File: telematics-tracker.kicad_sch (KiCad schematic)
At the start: 0 parts

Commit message: M2: mcu ERC-clean
mcu.kicad_sch: AT32F403ACGT7 with all 48 pins wired per handoff section 5,
verified 48/48 against the exported netlist by tools/checkpins.py.

Contents: 8 MHz HSE (Crystal_GND24 + 2x18pF), 32.768 kHz LSE (+2x6.8pF),
NRST 100nF, BOOT0 10k + solder-jumper to 3V3, BOOT1/PB2 10k pulldown,
VBAT via 0R from 3V3 + 100nF, VDDA ferrite + 1uF/100nF, 100nF per VDD pin
+ 4.7uF bulk, PC13 heartbeat LED, PB11 network LED via MMBT3904, U3
QMI8658B IMU on I2C1 with 2.2k pull-ups, and test points on SWD, both
debug UART lines, reset and the rails.

ERC: 0 errors. 51 warnings, all isolated_pin_label on root sheet pins that
only this sheet exposes so far; they resolve as storage/io/modem_rf land.

Generator fixes needed to get here (all now guarded in schgen.py):
  - power symbols must be in_bom/on_board yes, else their pins read as
    unconnected
  - power-symbol references must be unique project-wide, not per sheet
  - (property private ...) is valid in a schematic; stripping it caused a
    spurious lib_symbol_mismatch
  - added a net-collision detector: it caught R3 and FB1 stubs both landing
    on (88.9, 88.9), which had silently merged VBAT_MCU into 3V3 and shorted
    MCU pin 1 to pin 48

Co-Authored-By: Claude Fable 5 <noreply@anthropic.com>
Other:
- added sheet mcu (mcu.kicad_sch)
- note added: "Remove them when the power sheet is added."
- note added: "TEMPORARY: the PWR_FLAG symbols below mark rails that will be driven by"
- note added: "power.kicad_sch (not yet drawn - pending the buck selection decision)."

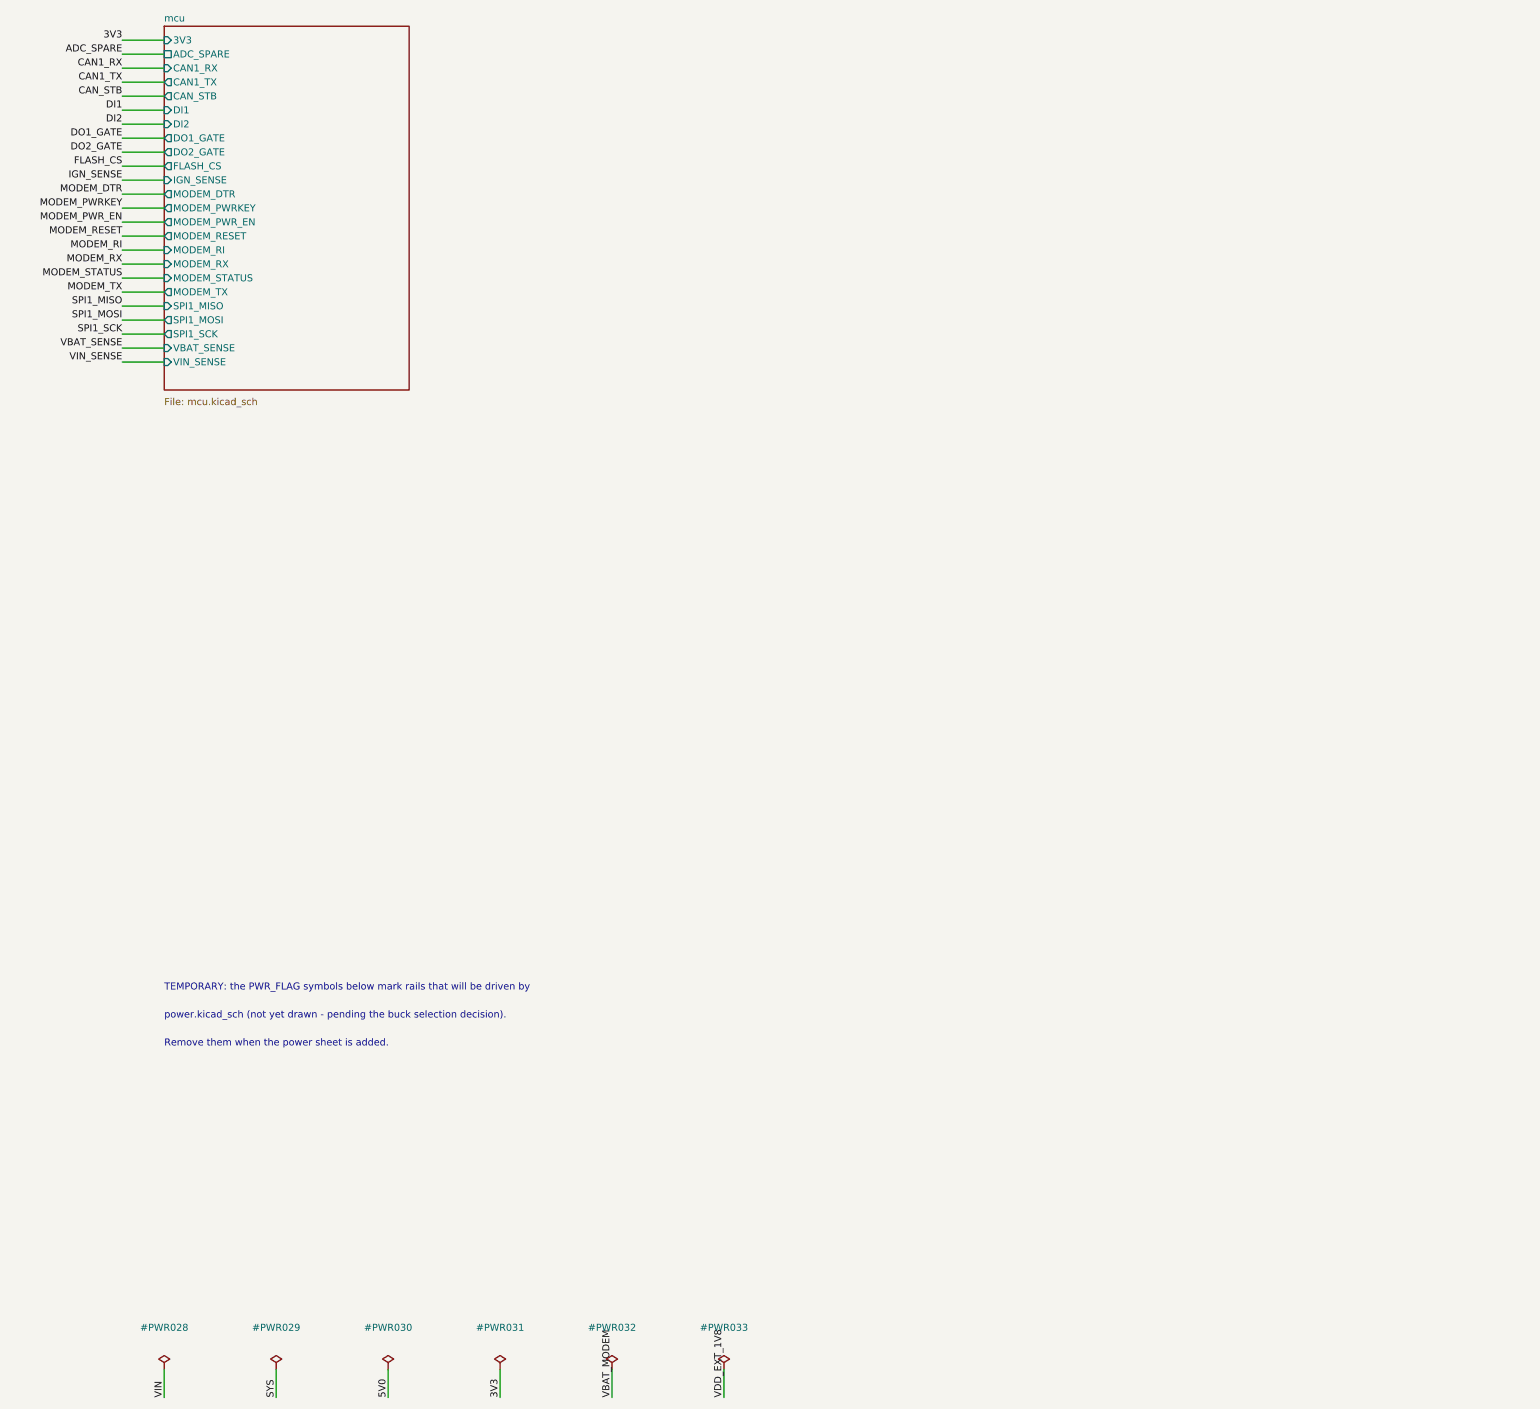
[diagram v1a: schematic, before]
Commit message: M2: storage ERC-clean
U7 GD25Q64ESIGR (C2831359, tape and reel per F-3) on SPI1: CS=PA4 via
FLASH_CS, SCK/MOSI/MISO to SPI1_*, WP# and HOLD# tied 3V3, 100nF + 1uF.
W25Q64JVSSIQ alternate recorded in the symbol's Alternate field.

Root inter-sheet plumbing switched from plain labels to global labels:
two same-named plain labels attached to sheet pins on different sheets are
reported dangling rather than merging. ERC 0 errors.

Co-Authored-By: Claude Fable 5 <noreply@anthropic.com>
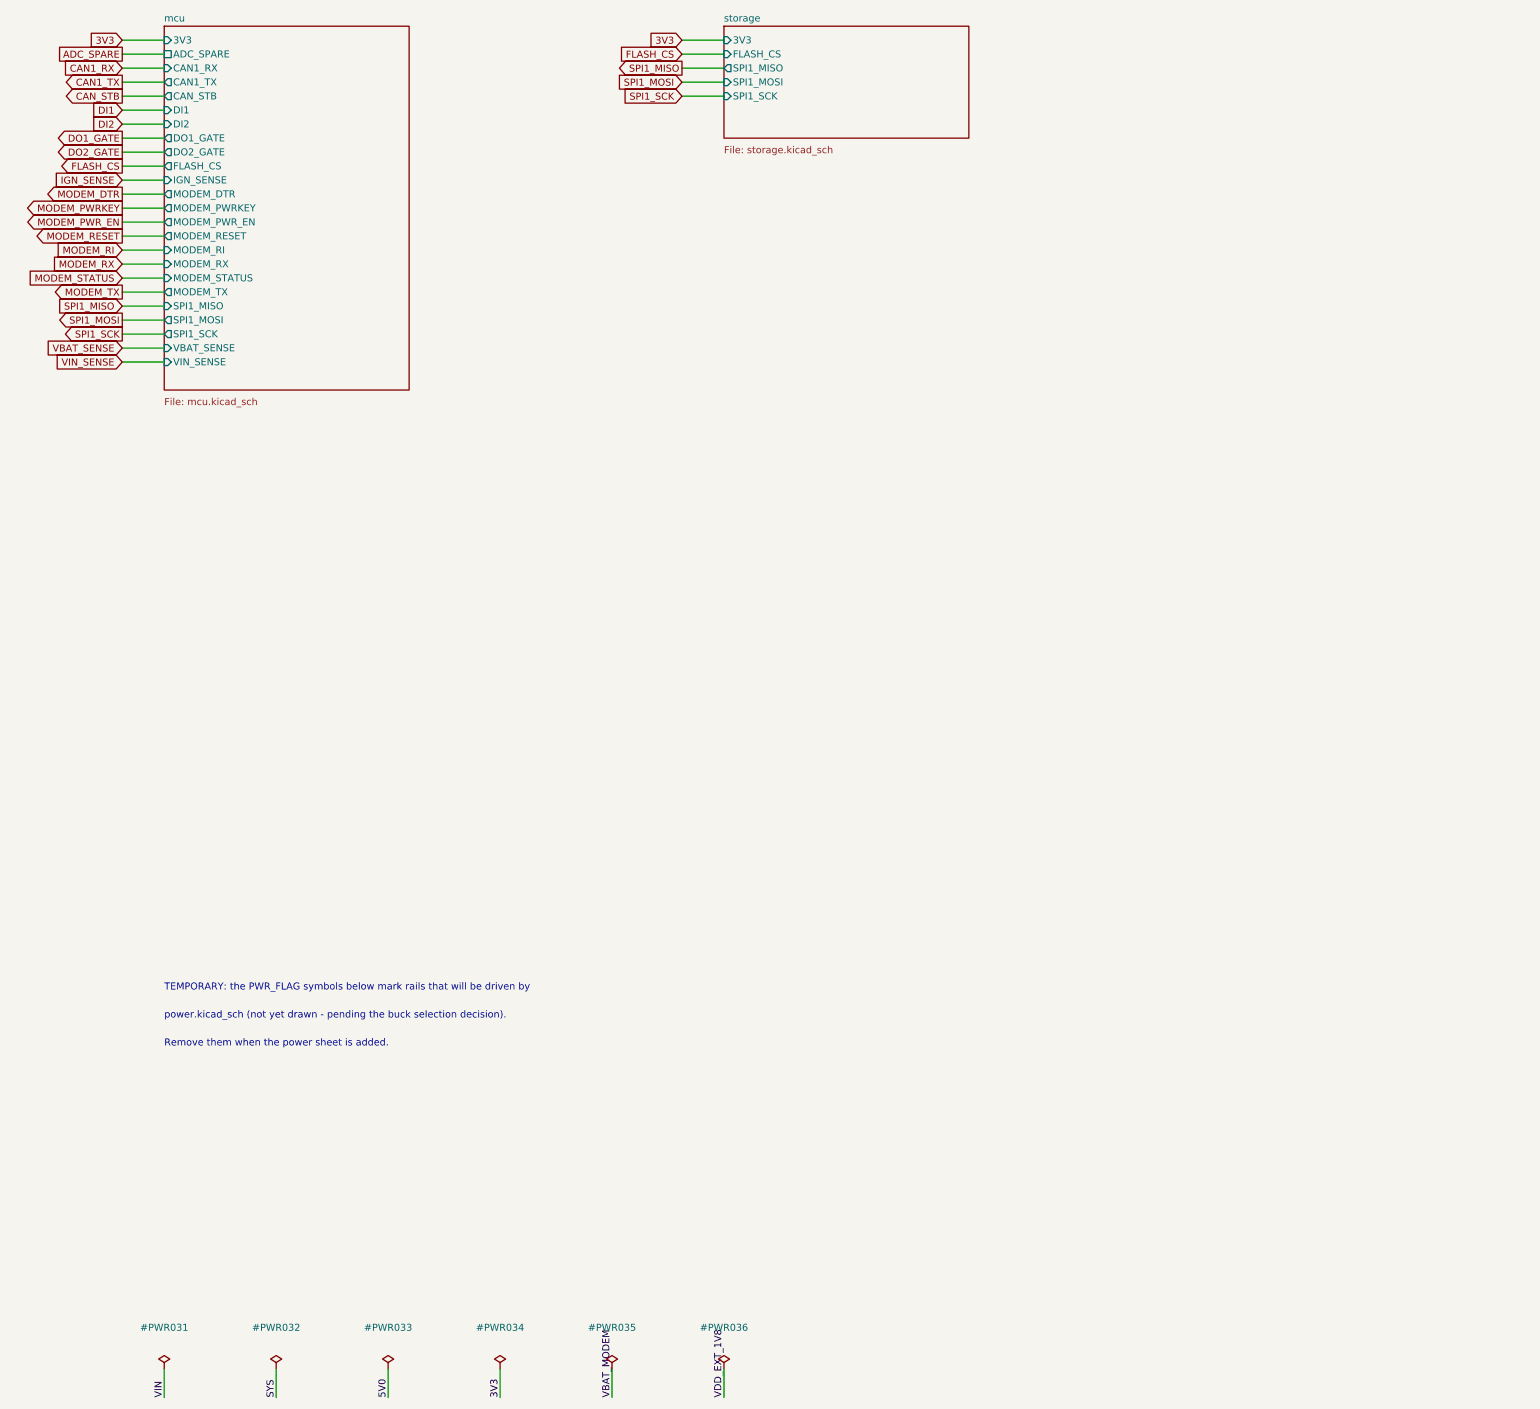
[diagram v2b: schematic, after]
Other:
- added sheet storage (storage.kicad_sch)

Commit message: M2: io ERC-clean
J1 12-pin harness (1 VIN, 2 GND, 3 IGN, 4 CANH, 5 CANL, 6 GND, 7 DI1,
8 DI2, 9 DO1, 10 DO2, 11/12 spare on test points).
CAN: SIT1051AT/3 with VIO=3V3 / VCC=5V0 / STB=PA15, CM choke + TVS at the
connector, split termination 2x60R + 4.7nF behind JP2 default OPEN.
DI1/DI2: 2x12k 1206 + BAV99 antiparallel + EL357N(D), 47k pull-up + 100nF.
DO1/DO2: NMOS low-side, 100R gate series, 10k pulldown, SS310 flyback to VIN.
Sensing: VIN and IGN 3x100k:9.1k + 100nF + BAV99 rail clamp; battery 1M:1M
from SYS; spare ADC divider fitted DNP.

ERC 0 errors. Two real faults were caught by new generator guards rather
than by eye:
  - the 100R DO gate resistor was shorted out by a second connection on the
    same FET gate pin (pin-connected-twice guard)
  - D3's GND stub and D4's CANL stub were collinear and overlapping, tying
    CANL to GND (new wire-overlap guard; ERC had shown it as
    multiple_net_names)

Parts still pending the in-stock sweep carry LCSC 'TBD-F8'.

Co-Authored-By: Claude Fable 5 <noreply@anthropic.com>
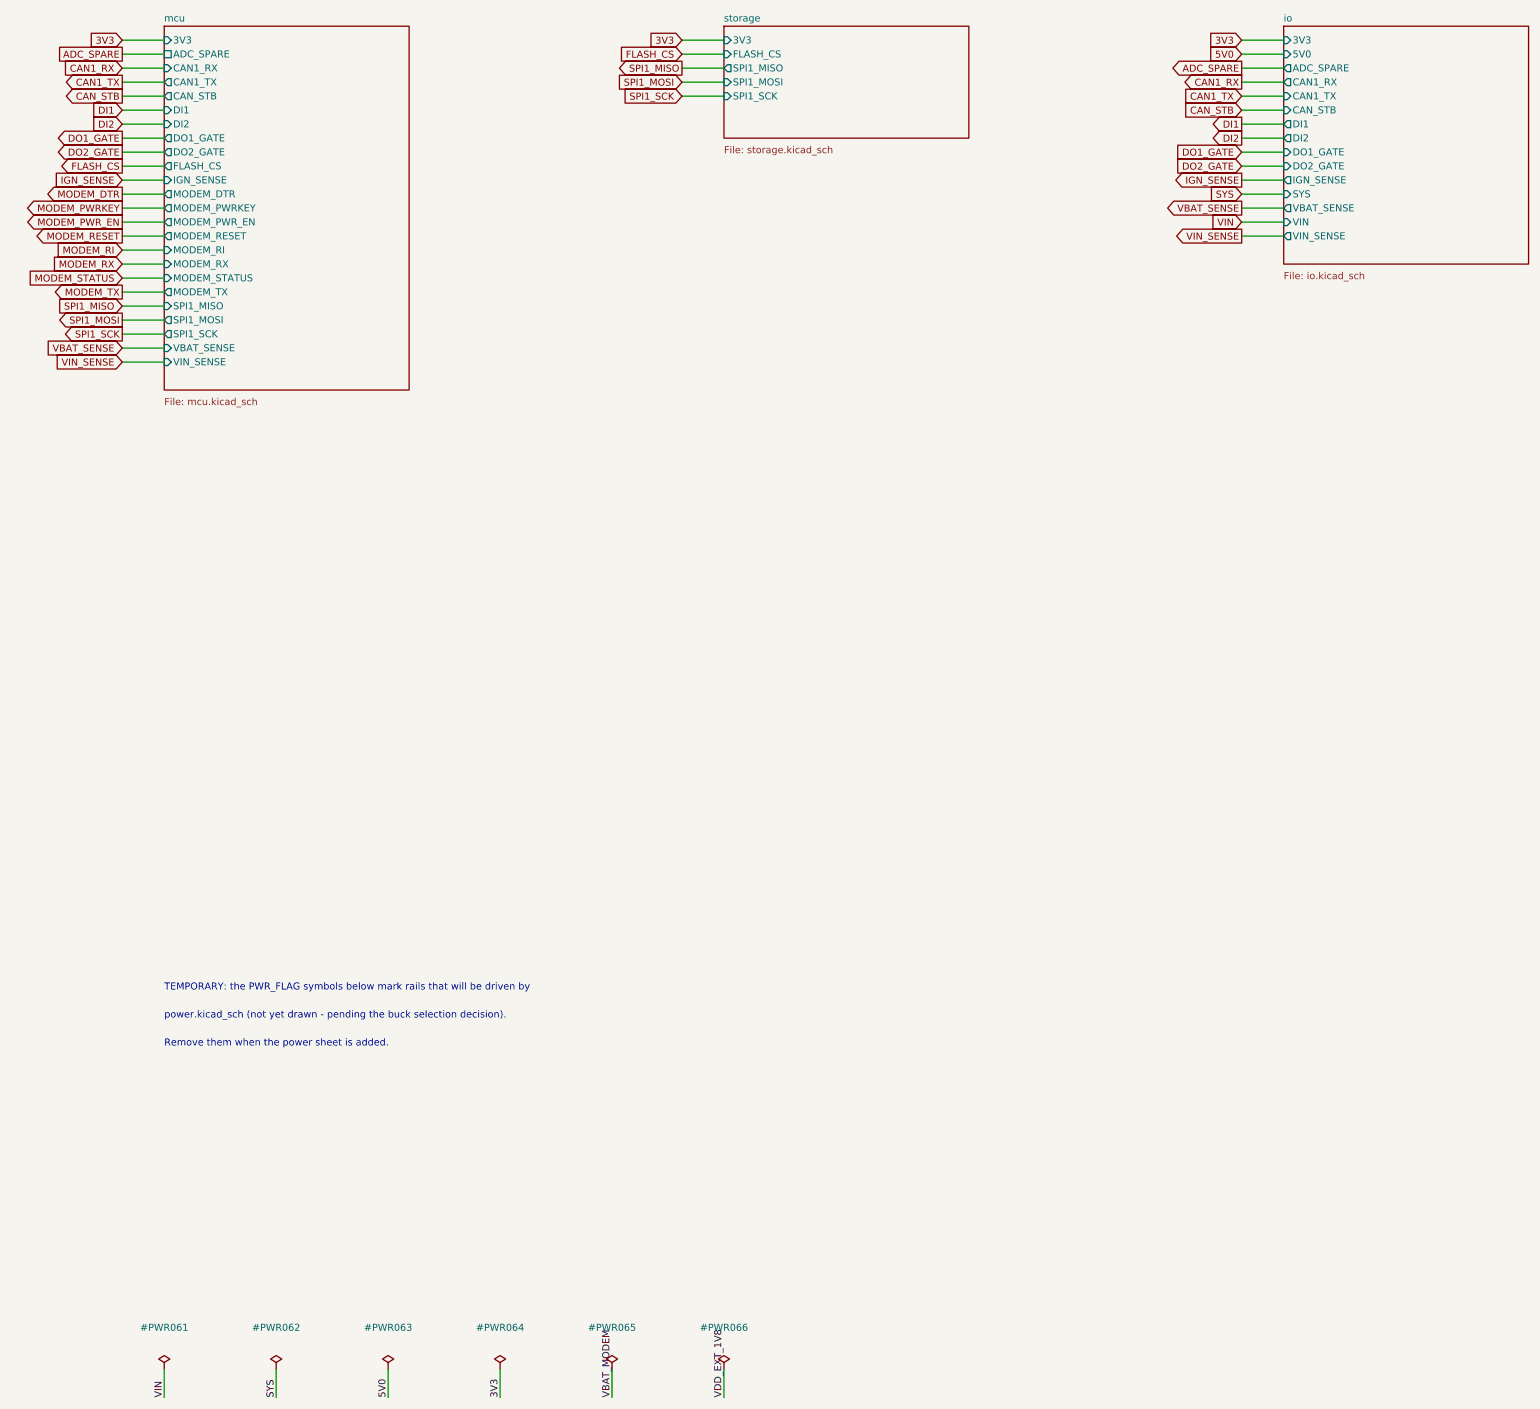
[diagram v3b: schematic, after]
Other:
- added sheet io (io.kicad_sch)
